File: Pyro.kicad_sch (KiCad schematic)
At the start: 36 parts, among them IC5 TPS259830ONRGER, J12 Conn_01x02_Male, Q2 BUK9M11-40EX, U10 SiC437BED-T1-GE3, U9 859-LTV-247

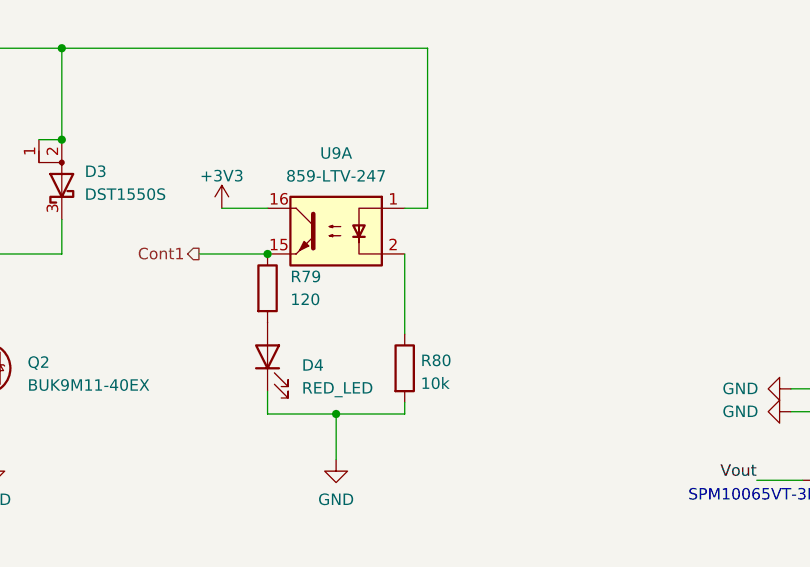
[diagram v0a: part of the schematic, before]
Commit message: tcmt1109 instead of ltv
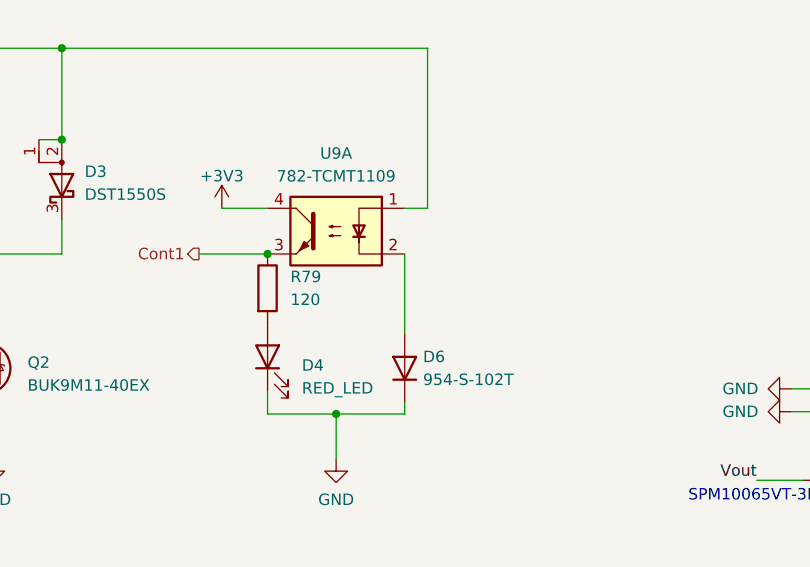
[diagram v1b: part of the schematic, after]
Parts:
- removed R80: 10k, Resistor_SMD:R_0603_1608Metric, symbol Device:R
- added D6: 954-S-102T, Diode_SMD:D_1206_3216Metric, symbol Device:D
- U9: value 859-LTV-247 -> 782-TCMT1109; footprint Package_DIP:SMDIP-4_W9.53mm -> iclr:SOIC127P700X230-4N
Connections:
- net +3V3: now also U9.4; no longer U9.16
- net Cont1: now also U9.3; no longer U9.15
- net GND: now also D6.1 (K)
- net at U9.2: now also D6.2 (A)
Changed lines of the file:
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@@
-	)
-	(symbol
-		(lib_id "Device:R")
-		(at 118.618 68.326 0)
-		(unit 1)
-		(exclude_from_sim no)
-		(in_bom yes)
-		(on_board yes)
-		(dnp no)
-		(fields_autoplaced yes)
-		(property "Reference" "R80"
-			(at 120.396 67.4913 0)
-			(effects
-				(font
-					(size 1.27 1.27)
-				)
-				(justify left)
-			)
-		)
-		(property "Value" "10k"
-			(at 120.396 70.0282 0)
-			(effects
-				(font
-					(size 1.27 1.27)
-				)
-				(justify left)
-			)
-		)
-		(property "Footprint" "Resistor_SMD:R_0603_1608Metric"
-			(at 116.84 68.326 90)
-			(effects
-				(font
-					(size 1.27 1.27)
-				)
-				(hide yes)
-			)
-		)
-		(property "Datasheet" "~"
-			(at 118.618 68.326 0)
-			(effects
-				(font
-					(size 1.27 1.27)
-				)
-				(hide yes)
-			)
-		)
-		(property "Description" ""
-			(at 118.618 68.326 0)
-			(effects
-				(font
-					(size 1.27 1.27)
-				)
-				(hide yes)
-			)
-		)
-		(pin "1"
-		)
-		(pin "2"
-		)
-		(instances
-			(project "Ricardo-Stark"
-				(path "/7db990e4-92e1-4f99-b4d2-435bbec1ba83/3c6662b6-8783-49dc-b944-3dc2b3e30a07"
-					(reference "R80")
-					(unit 1)
-				)
-			)
-		)
 	)
 	(symbol
@@
 			)
 		)
-		(property "Value" "859-LTV-247"
+		(property "Value" "782-TCMT1109"
 			(at 110.998 46.99 0)
 			(effects
@@
 			)
 		)
-		(property "Footprint" "Package_DIP:SMDIP-4_W9.53mm"
+		(property "Footprint" "iclr:SOIC127P700X230-4N"
 			(at 116.078 58.166 0)
 			(effects
@@
 			)
 		)
-		(property "Datasheet" "http://optoelectronics.liteon.com/upload/download/DS70-2009-0014/LTV-2X7%20sereis%20Mar17.PDF"
+		(property "Datasheet" "https://www.vishay.com/docs/83510/tcmt11.pdf"
 			(at 110.998 53.086 0)
 			(effects
@@
 		(pin "1"
 		)
-		(pin "15"
-		)
-		(pin "16"
+		(pin "3"
+		)
+		(pin "4"
 		)
 		(pin "2"
@@
 					(unit 1)
 				)
+			)
+		)
+	)
+	(symbol
+		(lib_id "Device:D")
+		(at 118.618 68.326 90)
+		(unit 1)
+		(exclude_from_sim no)
+		(in_bom yes)
+		(on_board yes)
+		(dnp no)
+		(fields_autoplaced yes)
+		(property "Reference" "D6"
+			(at 120.65 67.0559 90)
+			(effects
+				(font
+					(size 1.27 1.27)
+				)
+				(justify right)
+			)
+		)
+		(property "Value" "954-S-102T"
+			(at 120.65 69.5959 90)
+			(effects
+				(font
+					(size 1.27 1.27)
+				)
+				(justify right)
+			)
+		)
+		(property "Footprint" "Diode_SMD:D_1206_3216Metric"
+			(at 118.618 68.326 0)
+			(effects
+				(font
+					(size 1.27 1.27)
+				)
+				(hide yes)
+			)
+		)
+		(property "Datasheet" "https://www.mouser.co.uk/datasheet/2/362/P22-23-CRD-1729293.pdf"
+			(at 118.618 68.326 0)
+			(effects
+				(font
+					(size 1.27 1.27)
+				)
+				(hide yes)
+			)
+		)
+		(property "Description" "Diode"
+			(at 118.618 68.326 0)
+			(effects
+				(font
+					(size 1.27 1.27)
+				)
+				(hide yes)
+			)
+		)
+		(property "Sim.Device" "D"
+			(at 118.618 68.326 0)
+			(effects
+				(font
+					(size 1.27 1.27)
+				)
+				(hide yes)
+			)
+		)
+		(property "Sim.Pins" "1=K 2=A"
+			(at 118.618 68.326 0)
+			(effects
+				(font
+					(size 1.27 1.27)
+				)
+				(hide yes)
+			)
+		)
+		(pin "1"
+		)
+		(pin "2"
+		)
+		(instances
+			(project "Ricardo-Stark"
+				(path "/7db990e4-92e1-4f99-b4d2-435bbec1ba83/3c6662b6-8783-49dc-b944-3dc2b3e30a07"
+					(reference "D6")
+					(unit 1)
+				)
